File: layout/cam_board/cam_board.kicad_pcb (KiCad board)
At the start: 4 copper layers, 58 x 46 mm, 75 parts, among them J1 Debug, J2 USB Connector, J3 BATT_CONNECTOR, J4 LCD conn, J5 Stick conn, M1 MountingHole_2.1mm, M2 MountingHole_2.1mm, Q1 BSS138, SW1 BOOT0, SW2 NRST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

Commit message: Update layout and schematic
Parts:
- moved R6 2.91 mm to (103.0, 41.8), turned to -90 degrees
- moved R20 2.16 mm to (105.8, 40.8), turned to 180 degrees
- moved R10 0.88 mm to (119.7, 42.2)
- moved R12 0.70 mm to (119.7, 46.2)
- moved R9 0.53 mm to (119.7, 47.8)
- moved SW3 0.50 mm to (75.4, 57.5)
- moved C15 0.25 mm to (109.5, 66.2)
- moved C2 0.25 mm to (99.9, 66.8)
- moved C5 0.25 mm to (101.0, 66.8)
- moved R11 0.24 mm to (119.7, 40.5)
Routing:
- net VIN: track 70.7 -> 36.9 mm, vias 13 -> 14
- net GND: track 102.8 -> 93.1 mm, vias 50 -> 52
- net VOUT: track 42.7 -> 39.2 mm
- net BATTLVL: track 58.6 -> 60.3 mm
- net +3V3: track 53.2 -> 54.4 mm, vias 16 -> 17
- net BATTLVL_READ: track 30.7 -> 30.0 mm

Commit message: Update layout and schematic
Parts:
- added C6: 100nF, Capacitor_SMD:C_0402_1005Metric_Pad0.74x0.62mm_HandSolder, F.Cu at (83.1, 46.5)
- added R23: 10k, Resistor_SMD:R_0603_1608Metric_Pad0.98x0.95mm_HandSolder, F.Cu at (86.8, 50.2)
- added R24: 10k, Resistor_SMD:R_0603_1608Metric_Pad0.98x0.95mm_HandSolder, F.Cu at (85.2, 51.7)
- added U3: M24C16-RMN6TP, A_Custom:SOIC127P600X175-8N, F.Cu at (79.8, 50.2)
- SW1, SW2, SW4: footprint Button_Switch_SMD:SW_DIP_SPSTx01_Slide_9.78x4.72mm_W8.61mm_P2.54mm -> Button_Switch_SMD:SW_DIP_SPSTx01_Slide_6.7x4.1mm_W8.61mm_P2.54mm_LowProfile
- moved SW1 4.49 mm to (76.0, 40.9)
- moved C12 4.49 mm to (79.4, 46.4)
- moved R2 4.49 mm to (79.4, 44.6)
- moved J2 1.48 mm to (125.4, 68.6)
- moved R5 1.31 mm to (117.8, 66.8)
- moved SW3 0.81 mm to (75.1, 58.2)
- moved C13 0.75 mm to (79.2, 74.2)
- moved R1 0.75 mm to (79.3, 72.5)
- moved SW2 0.75 mm to (76.0, 68.7)
- moved C18 0.62 mm to (79.5, 56.1)
- moved R7 0.62 mm to (81.1, 56.1)
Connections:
- U1 pad 41: unconnected-(U1-PB5-Pad41) -> EEPROM_NWC
- U1 pad 42: unconnected-(U1-PB6-Pad42) -> EEPROM_SCL
- U1 pad 43: unconnected-(U1-PB7-Pad43) -> EEPROM_SDA
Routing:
- net EEPROM_NWC: track 0.00 -> 22.5 mm
- net EEPROM_SCL: track 0.00 -> 21.4 mm
- net EEPROM_SDA: track 0.00 -> 18.1 mm
- net GND: track 93.1 -> 99.5 mm, vias 52 -> 129
- net +3V3: track 54.4 -> 60.0 mm, vias 17 -> 19
- net BOOT0: track 25.7 -> 31.0 mm
- net Net-(U2-GND): track 27.4 -> 30.2 mm
- net Net-(J2-D--PadA7): track 12.8 -> 14.2 mm
- net Net-(J2-CC1): track 2.70 -> 4.19 mm
- net Net-(J2-D+-PadA6): track 13.0 -> 14.5 mm
- net USRBUTTON: track 29.5 -> 28.3 mm
- net Net-(D5-A): track 13.9 -> 13.0 mm
- net NRST: track 71.9 -> 72.6 mm
- net SWD+5V: track 6.29 -> 5.74 mm
- net Net-(J2-CC2): track 2.15 -> 2.70 mm
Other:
- board size 58 x 46 mm -> 59 x 46 mm

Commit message: Update layout and schematic
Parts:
- added JP1: Prog1, Jumper:SolderJumper-3_P1.3mm_Open_RoundedPad1.0x1.5mm_NumberLabels, F.Cu at (108.5, 33.8)
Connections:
- C21 pad 2: VIN -> Net-(JP1-B)
- U5 pad 18: VIN -> Net-(JP1-B)
- U5 pad 19: VIN -> Net-(JP1-B)
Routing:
- net Net-(JP1-B): track 0.00 -> 10.3 mm
- net VOUT: track 39.2 -> 46.3 mm
- net VIN: track 36.9 -> 32.5 mm
- net GND: track 99.5 -> 99.7 mm, vias 129 -> 132
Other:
- board size 59 x 46 mm -> 59 x 47 mm

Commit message: Update layout and schematic
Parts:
- removed D2, D3: D_Schottky, Diode_SMD:D_0603_1608Metric_Pad1.05x0.95mm_HandSolder
- removed Q1: BSS138, Package_TO_SOT_SMD:SOT-23_Handsoldering
- C6: footprint Capacitor_SMD:C_0402_1005Metric_Pad0.74x0.62mm_HandSolder -> Capacitor_SMD:C_0603_1608Metric_Pad1.08x0.95mm_HandSolder
- J1: value Debug -> Conn_01x04_Pin; footprint Connector_PinHeader_1.27mm:PinHeader_1x06_P1.27mm_Vertical -> Connector_PinHeader_1.27mm:PinHeader_1x04_P1.27mm_Vertical
- JP1: value Prog1 -> Battery Bypass
- R17: value 100k -> 100M
- R18: value 220k -> 220M
- moved J1 2.41 mm to (126.0, 58.0)
- moved R18 1.20 mm to (120.0, 54.2)
- moved M2 0.75 mm to (115.0, 74.5)
- moved C6 0.18 mm to (83.2, 46.5)
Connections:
- C14 pad 2: USB+5V -> VIN
- C15 pad 2: USB+5V -> VIN
- D5 pad 1: USB+5V -> VIN
- J1 pad 1: GND -> SWCLK
- J1 pad 2: SWD+5V -> SWDIO
- J1 pad 3: SWCLK -> SWO
- J1 pad 4: SWDIO -> NRST
- R18 pad 1: Net-(Q1-D) -> GND
- U1 pad 25: BATTLVL_READ -> unconnected-(U1-PB12-Pad25)
- U2 pad 5: USB+5V -> VIN
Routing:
- net BATTLVL_READ: track 30.0 -> 0.00 mm, vias 2 -> 0
- net VIN: track 32.5 -> 55.3 mm, vias 14 -> 15
- net USB+5V: track 22.4 -> 0.00 mm
- net SWD+5V: track 5.74 -> 0.00 mm
- net Net-(Q1-D): track 2.68 -> 0.00 mm
- net BATTLVL: track 60.3 -> 57.9 mm
- net GND: track 99.7 -> 97.6 mm, vias 132 -> 124
- net SWCLK: track 28.3 -> 27.1 mm
- net BATTCHARGE: track 44.7 -> 45.3 mm
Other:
- board size 59 x 47 mm -> 60 x 45 mm
- board text added: "EEPROM"
- board text added: "ESD"
- board text removed: "+5V"

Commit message: Update layout and schematic
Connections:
- U1 pad 34: SWCLK -> SWDIO
- U1 pad 37: SWDIO -> SWCLK
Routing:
- net SWCLK: track 27.1 -> 30.6 mm
- net SWDIO: track 29.9 -> 31.2 mm
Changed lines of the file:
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@@
 		(tags "SOT-23-6 Handsoldering")
 		(property "Reference" "U2"
-			(at 0 0 0)
+			(at 1 -2.65 0)
 			(layer "F.SilkS")
 			(effects
@@
 			(net 62 "Net-(JP1-B)")
 			(pinfunction "B")
-			(pintype "passive")
+			(pintype "power_out")
 			(zone_connect 2)
 			(thermal_bridge_angle 45)
@@
 			(roundrect_rratio 0.25)
 			(net 48 "Net-(U5-VPCC)")
-			(pintype "power_out")
+			(pintype "passive")
 		)
 		(pad "2" smd roundrect
@@
 			(roundrect_rratio 0.25)
 			(net 64 "VIN")
-			(pintype "power_out")
+			(pintype "passive")
 		)
 		(embedded_fonts no)
@@
 			(layers "F.Cu" "F.Mask" "F.Paste")
 			(roundrect_rratio 0.25)
-			(net 16 "SWCLK")
+			(net 9 "SWDIO")
 			(pinfunction "PA13")
 			(pintype "bidirectional")
@@
 			(layers "F.Cu" "F.Mask" "F.Paste")
 			(roundrect_rratio 0.25)
-			(net 9 "SWDIO")
+			(net 16 "SWCLK")
 			(pinfunction "PA14")
 			(pintype "bidirectional")
@@
 	)
 	(gr_text "ESD"
-		(at 109 71.5 0)
+		(at 110 71.5 0)
 		(layer "F.SilkS")
 		(effects
@@
 	)
 	(segment
-		(start 127.199 61.25)
-		(end 125.699 62.75)
+		(start 126 54.19)
+		(end 126.94 54.19)
+		(width 0.25)
+		(layer "B.Cu")
+		(net 6)
+	)
+	(segment
+		(start 126.94 54.19)
+		(end 127.374 54.624)
 		(width 0.25)
 		(layer "B.Cu")
@@
 	)
 	(segment
-		(start 126.34 54.19)
-		(end 127.199 55.049)
+		(start 127.374 54.624)
+		(end 127.374 61.075)
 		(width 0.25)
 		(layer "B.Cu")
@@
 	)
 	(segment
-		(start 84.5 65.75)
-		(end 85.5 65.75)
+		(start 101 68.5)
+		(end 95.420211 62.920211)
 		(width 0.25)
 		(layer "B.Cu")
@@
 	)
 	(segment
-		(start 125.699 62.75)
-		(end 110.67672 62.75)
+		(start 95.420211 62.920211)
+		(end 90.011173 62.920211)
 		(width 0.25)
 		(layer "B.Cu")
@@
 	)
 	(segment
-		(start 101 68.5)
-		(end 95.420211 62.920211)
+		(start 84.5 65.75)
+		(end 85.5 65.75)
 		(width 0.25)
 		(layer "B.Cu")
@@
 	)
 	(segment
-		(start 88.329789 62.920211)
-		(end 90.011173 62.920211)
+		(start 125.699 62.75)
+		(end 110.67672 62.75)
 		(width 0.25)
 		(layer "B.Cu")
@@
 	)
 	(segment
-		(start 90.580933 62.350451)
+		(start 88.329789 62.920211)
 		(end 90.011173 62.920211)
 		(width 0.25)
@@
 	)
 	(segment
-		(start 95.420211 62.920211)
-		(end 90.011173 62.920211)
+		(start 127.374 61.075)
+		(end 125.699 62.75)
 		(width 0.25)
 		(layer "B.Cu")
@@
 	)
 	(segment
-		(start 127.199 55.049)
-		(end 127.199 61.25)
+		(start 90.580933 62.350451)
+		(end 90.011173 62.920211)
 		(width 0.25)
 		(layer "B.Cu")
@@
 	)
 	(segment
-		(start 126 54.19)
-		(end 126.34 54.19)
-		(width 0.25)
-		(layer "B.Cu")
-		(net 6)
-	)
-	(segment
 		(start 97.375 64.8475)
 		(end 97.375 68.088566)
@@
 	)
 	(segment
-		(start 98.875 56.375)
-		(end 98.875 57.9725)
+		(start 99.5625 59.66)
+		(end 102.84 59.66)
 		(width 0.25)
 		(layer "F.Cu")
@@
 	)
 	(segment
-		(start 98.999 56.251)
-		(end 98.875 56.375)
+		(start 102.84 59.66)
+		(end 103.25 59.25)
 		(width 0.25)
 		(layer "F.Cu")
 		(net 9)
 	)
+	(via
+		(at 103.25 59.25)
+		(size 0.8)
+		(drill 0.4)
+		(layers "F.Cu" "B.Cu")
+		(net 9)
+	)
 	(segment
-		(start 100.75 55.5)
-		(end 99.999 56.251)
+		(start 125.25 59.5)
+		(end 126.5 59.5)
 		(width 0.25)
-		(layer "F.Cu")
+		(layer "B.Cu")
 		(net 9)
 	)
 	(segment
-		(start 99.999 56.251)
-		(end 98.999 56.251)
+		(start 126.923 59.077)
+		(end 126.923 57.173)
 		(width 0.25)
-		(layer "F.Cu")
+		(layer "B.Cu")
 		(net 9)
 	)
-	(via
-		(at 100.75 55.5)
-		(size 0.8)
-		(drill 0.4)
-		(layers "F.Cu" "B.Cu")
+	(segment
+		(start 103.25 59.25)
+		(end 103.75 58.75)
+		(width 0.25)
+		(layer "B.Cu")
 		(net 9)
 	)
 	(segment
-		(start 103 55.25)
-		(end 102.75 55.5)
+		(start 124.5 58.75)
+		(end 125.25 59.5)
 		(width 0.25)
 		(layer "B.Cu")
@@
 	)
 	(segment
-		(start 126.2 56.59)
-		(end 125.86 56.59)
+		(start 126.5 59.5)
+		(end 126.923 59.077)
 		(width 0.25)
 		(layer "B.Cu")
@@
 	)
 	(segment
-		(start 102.75 55.5)
-		(end 100.75 55.5)
+		(start 126.48 56.73)
+		(end 126 56.73)
 		(width 0.25)
 		(layer "B.Cu")
@@
 	)
 	(segment
-		(start 124.52 55.25)
-		(end 103 55.25)
+		(start 103.75 58.75)
+		(end 124.5 58.75)
 		(width 0.25)
 		(layer "B.Cu")
@@
 	)
 	(segment
-		(start 125.86 56.59)
-		(end 124.52 55.25)
+		(start 126.923 57.173)
+		(end 126.48 56.73)
 		(width 0.25)
 		(layer "B.Cu")
@@
 	)
 	(segment
-		(start 103.2 59.2)
-		(end 102 59.2)
+		(start 100.737427 54.762573)
+		(end 98.875 56.625)
 		(width 0.25)
 		(layer "F.Cu")
@@
 	)
 	(segment
-		(start 102 59.2)
-		(end 101.54 59.66)
+		(start 101.749839 54.762573)
+		(end 100.737427 54.762573)
 		(width 0.25)
 		(layer "F.Cu")
@@
 	)
 	(segment
-		(start 101.54 59.66)
-		(end 99.5625 59.66)
+		(start 98.875 56.625)
+		(end 98.875 57.9725)
 		(width 0.25)
 		(layer "F.Cu")
@@
 	)
 	(via
-		(at 103.2 59.2)
+		(at 101.749839 54.762573)
 		(size 0.8)
 		(drill 0.4)
@@
 	)
 	(segment
-		(start 112.70072 58.526)
-		(end 112.09928 58.526)
-		(width 0.25)
-		(layer "B.Cu")
-		(net 16)
-	)
-	(segment
-		(start 112.72672 58.5)
-		(end 112.70072 58.526)
-		(width 0.25)
-		(layer "B.Cu")
-		(net 16)
-	)
-	(segment
-		(start 117.448 58.5)
-		(end 112.72672 58.5)
-		(width 0.25)
-		(layer "B.Cu")
-		(net 16)
-	)
-	(segment
-		(start 126 58)
-		(end 125.5 58.5)
+		(start 101.749839 54.762573)
+		(end 122.762573 54.762573)
 		(width 0.25)
 		(layer "B.Cu")
@@
 	)
 	(segment
-		(start 117.474 58.526)
-		(end 117.448 58.5)
-		(width 0.25)
-		(layer "B.Cu")
-		(net 16)
-	)
-	(segment
-		(start 112.09928 58.526)
-		(end 112.07328 58.5)
-		(width 0.25)
-		(layer "B.Cu")
-		(net 16)
-	)
-	(segment
-		(start 103.9 58.5)
-		(end 103.2 59.2)
-		(width 0.25)
-		(layer "B.Cu")
-		(net 16)
-	)
-	(segment
-		(start 125.5 58.5)
-		(end 117.5 58.5)
-		(width 0.25)
-		(layer "B.Cu")
-		(net 16)
-	)
-	(segment
-		(start 112.07328 58.5)
-		(end 103.9 58.5)
+		(start 122.762573 54.762573)
+		(end 126 58)
 		(width 0.25)
 		(layer "B.Cu")
@@
 	)
 	(segment
-		(start 99.913247 54.5)
+		(start 100.650594 53.762653)
 		(end 97.875 56.538247)
 		(width 0.25)
@@
 	)
 	(segment
-		(start 97.875 56.538247)
-		(end 97.875 57.9725)
+		(start 101.762653 53.762653)
+		(end 100.650594 53.762653)
 		(width 0.25)
 		(layer "F.Cu")
@@
 	)
 	(segment
-		(start 101.75 54.5)
-		(end 99.913247 54.5)
+		(start 97.875 56.538247)
+		(end 97.875 57.9725)
 		(width 0.25)
 		(layer "F.Cu")
@@
 	)
 	(via
-		(at 101.75 54.5)
+		(at 101.762653 53.762653)
 		(size 0.8)
 		(drill 0.4)
@@
 	)
 	(segment
-		(start 125.86 55.32)
-		(end 126.2 55.32)
+		(start 101.775306 54)
+		(end 102.012653 53.762653)
 		(width 0.25)
 		(layer "B.Cu")
@@
 	)
 	(segment
-		(start 102 54.25)
-		(end 124.79 54.25)
+		(start 124.302653 53.762653)
+		(end 125.86 55.32)
 		(width 0.25)
 		(layer "B.Cu")
@@
 	)
 	(segment
-		(start 101.75 54.5)
-		(end 102 54.25)
+		(start 102.012653 53.762653)
+		(end 124.302653 53.762653)
 		(width 0.25)
 		(layer "B.Cu")
@@
 	)
 	(segment
-		(start 124.79 54.25)
-		(end 125.86 55.32)
+		(start 125.86 55.32)
+		(end 126.2 55.32)
 		(width 0.25)
 		(layer "B.Cu")

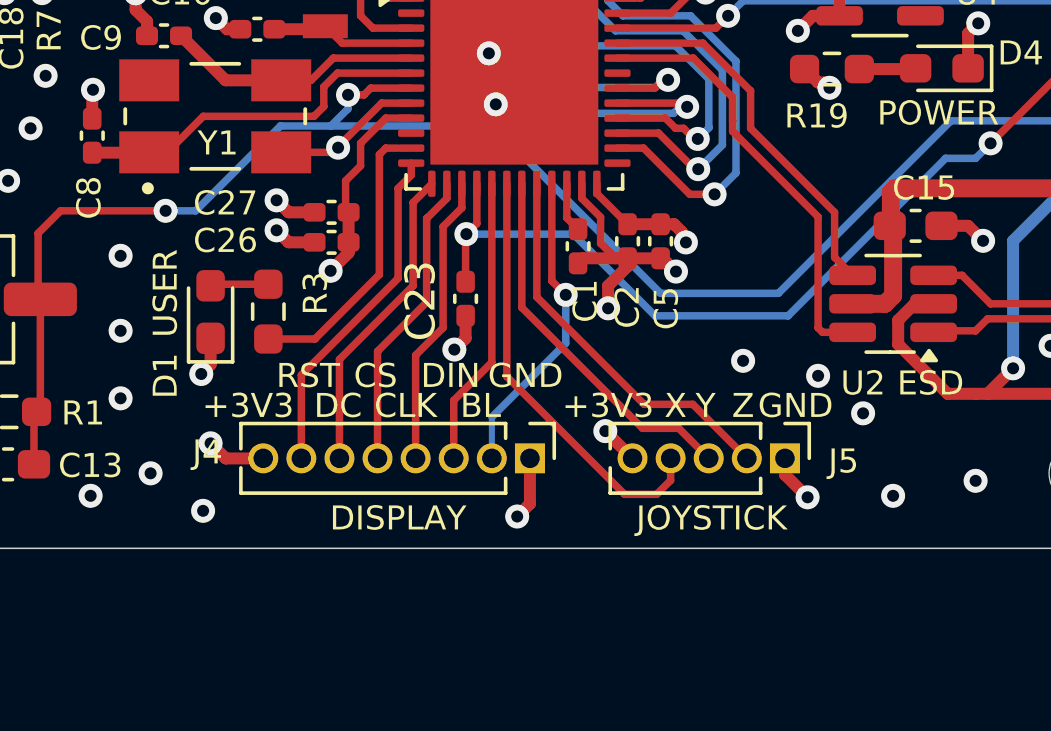
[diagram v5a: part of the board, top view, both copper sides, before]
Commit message: Fix menu, add missing pull-up
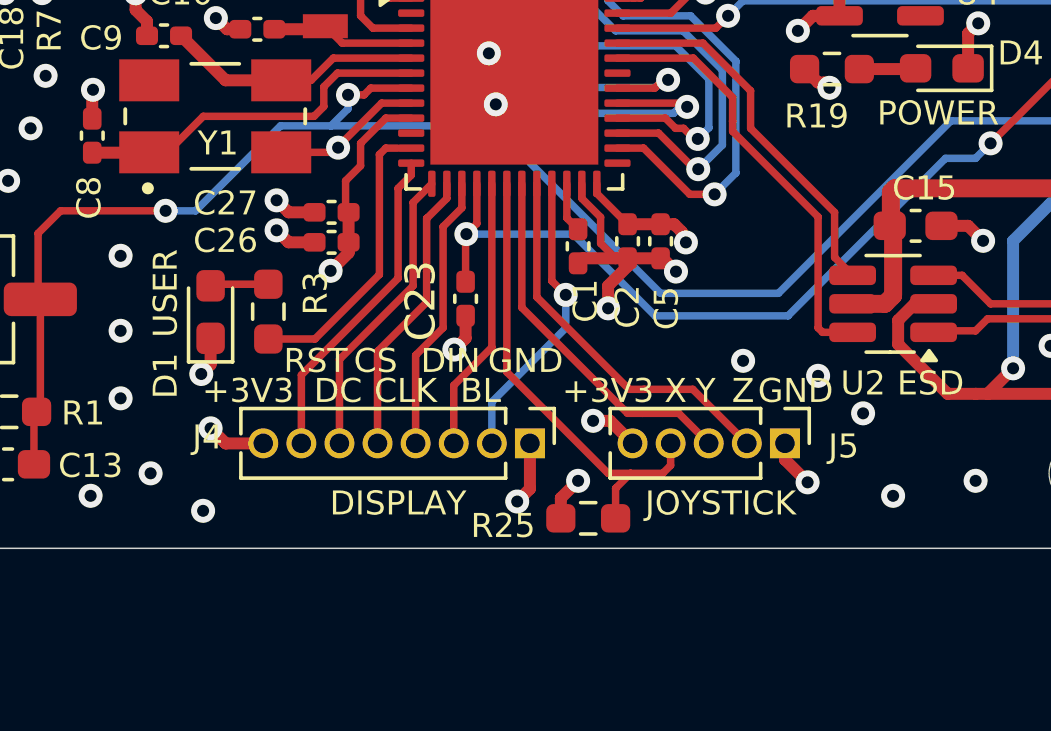
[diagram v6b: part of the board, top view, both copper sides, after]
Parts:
- added R25: 1k, Resistor_SMD:R_0603_1608Metric_Pad0.98x0.95mm_HandSolder, F.Cu at (98.6, 76.0)
- moved J4 0.50 mm to (96.6, 73.5)
- moved J5 0.50 mm to (105.1, 73.5)
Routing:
- net +3V3: track 59.8 -> 61.6 mm, vias 19 -> 20
- net STICK_X: track 14.4 -> 15.7 mm
- net DIN: track 9.68 -> 9.18 mm
- net DC: track 10.4 -> 9.93 mm
- net CS: track 10.1 -> 9.62 mm
- net CLK: track 9.79 -> 9.29 mm
- net BL: track 10.4 -> 9.86 mm

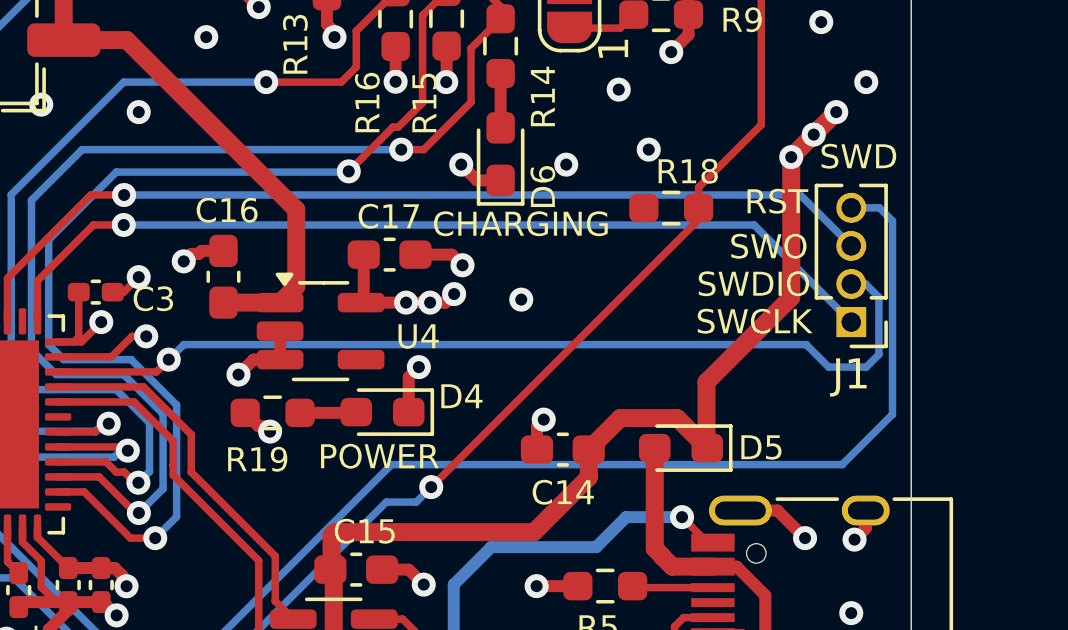
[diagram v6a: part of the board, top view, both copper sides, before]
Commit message: Prepare USB and fix missing GND line in layout
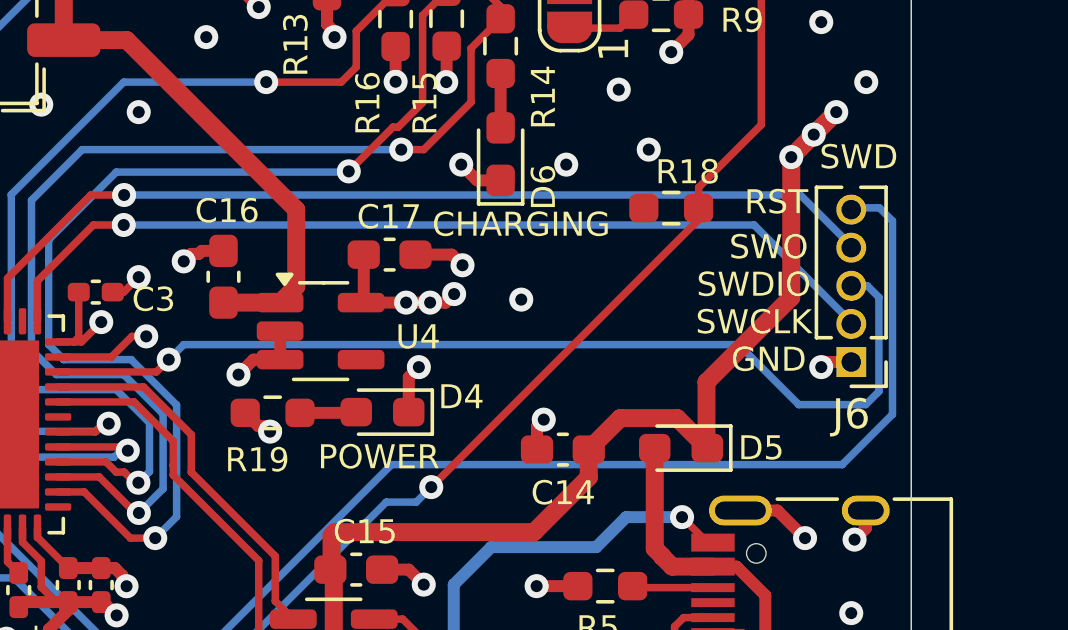
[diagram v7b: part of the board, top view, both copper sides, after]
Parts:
- removed J1: Conn_01x04_Pin, Connector_PinHeader_1.27mm:PinHeader_1x04_P1.27mm_Vertical
- added J6: Conn_01x05_Pin, Connector_PinHeader_1.27mm:PinHeader_1x05_P1.27mm_Vertical, F.Cu at (126.0, 59.3)
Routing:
- net SWDIO: track 31.2 -> 33.0 mm
- net GND: track 97.6 -> 98.7 mm, vias 124 -> 125
